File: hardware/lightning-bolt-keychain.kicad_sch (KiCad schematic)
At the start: 14 parts, among them J1 USB-C Power In

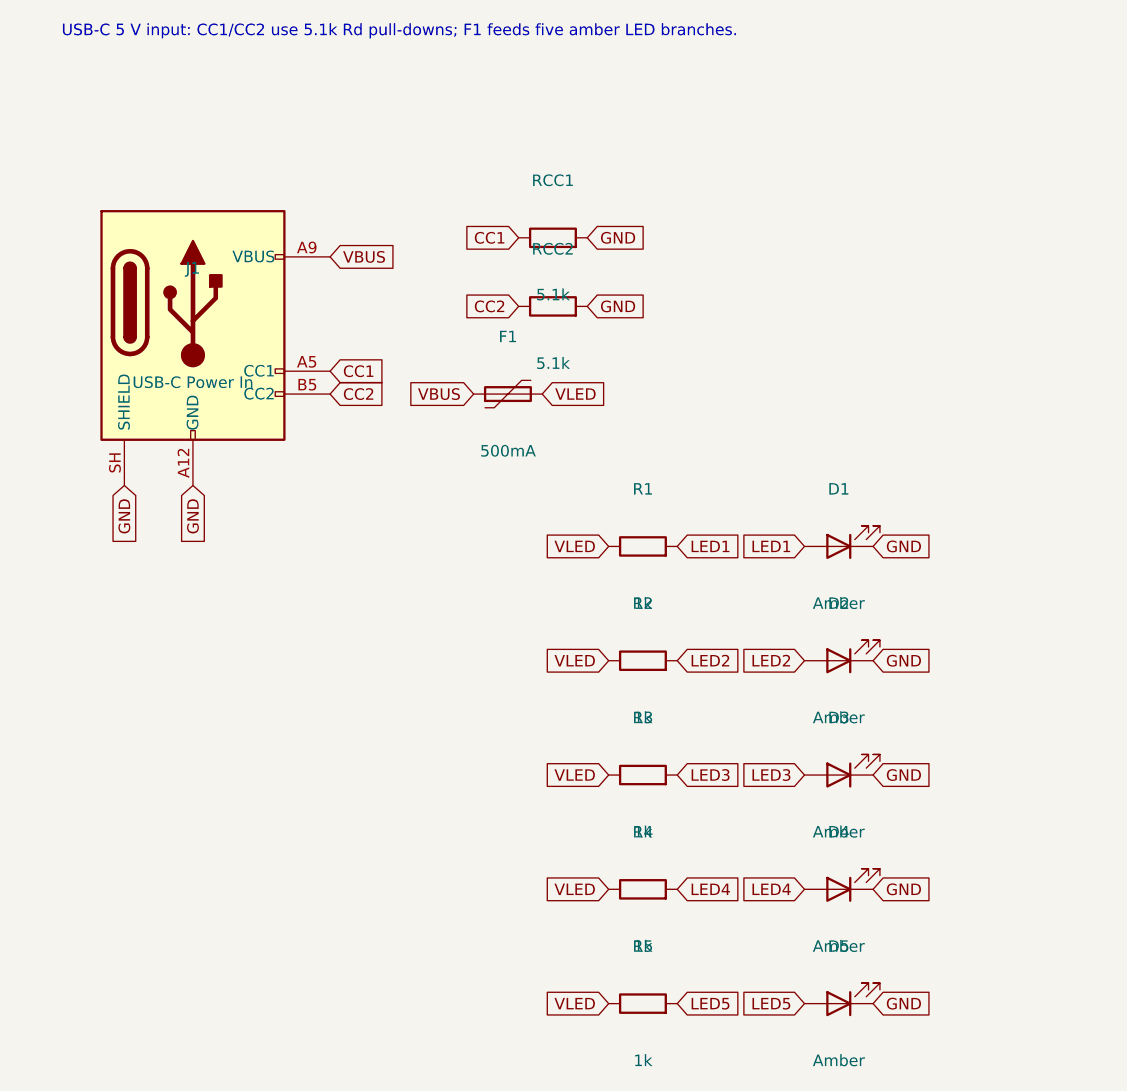
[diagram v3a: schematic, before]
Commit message: Refine bolt outline and schematic readability
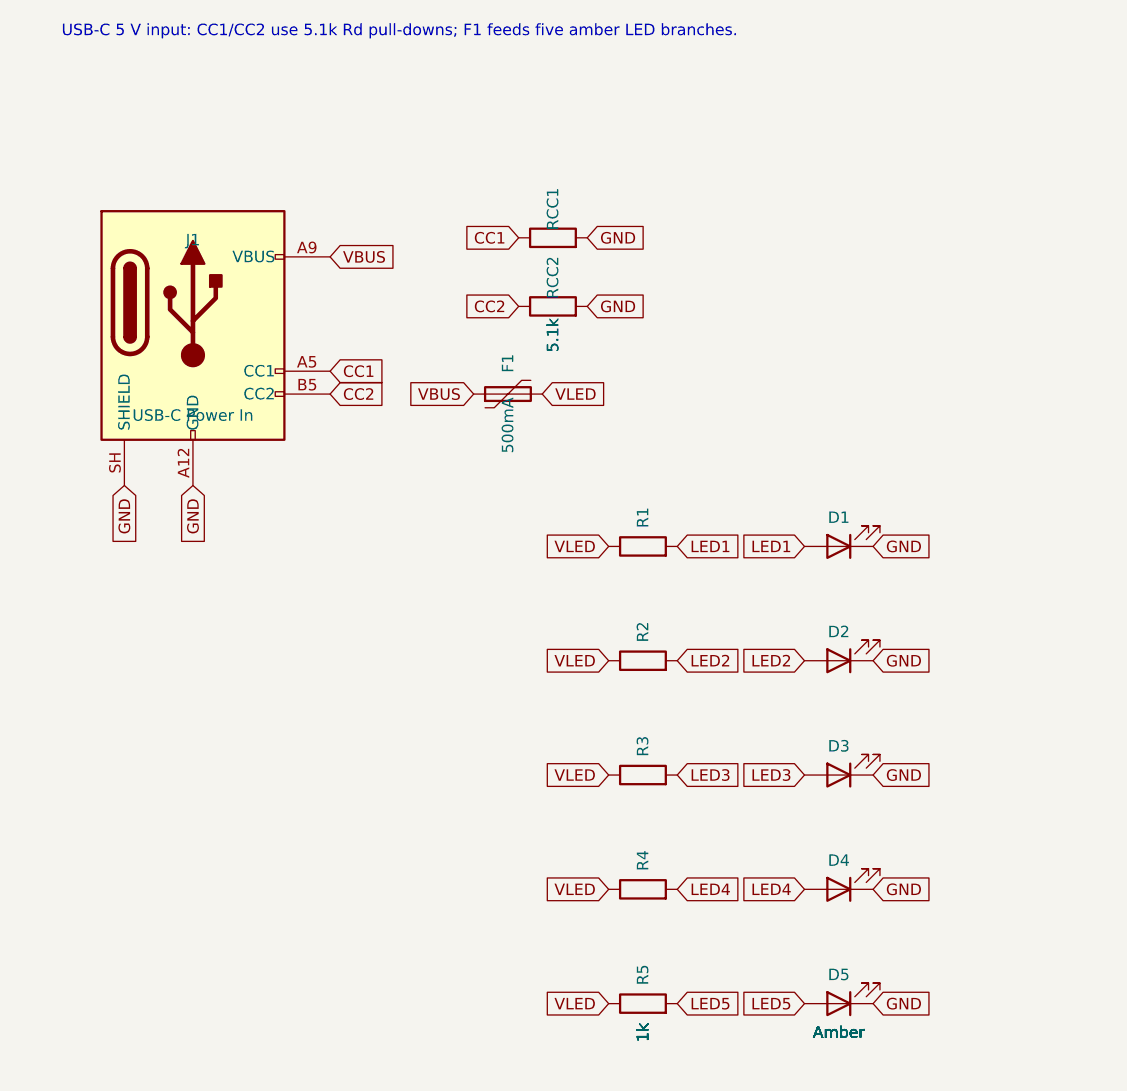
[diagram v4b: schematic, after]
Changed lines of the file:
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@@
   (symbol (lib_id "Connector:USB_C_Receptacle_PowerOnly_6P") (at 40.00 58.00 0) (unit 1)
     (in_bom yes) (on_board yes) (dnp no)
-    (property "Reference" "J1" (at 40.00 51.65 0)
+    (property "Reference" "J1" (at 40.00 48.50 0)
       (effects (font (size 1.27 1.27)))
     )
-    (property "Value" "USB-C Power In" (at 40.00 64.35 0)
+    (property "Value" "USB-C Power In" (at 40.00 68.00 0)
       (effects (font (size 1.27 1.27)))
     )
@@
   (symbol (lib_id "Device:Polyfuse") (at 75.00 65.62 90) (unit 1)
     (in_bom yes) (on_board yes) (dnp no)
-    (property "Reference" "F1" (at 75.00 59.27 90)
+    (property "Reference" "F1" (at 75.00 62.20 0)
       (effects (font (size 1.27 1.27)))
     )
-    (property "Value" "500mA" (at 75.00 71.97 90)
+    (property "Value" "500mA" (at 75.00 69.10 0)
       (effects (font (size 1.27 1.27)))
     )
@@
   (symbol (lib_id "Device:R") (at 80.00 48.26 90) (unit 1)
     (in_bom yes) (on_board yes) (dnp no)
-    (property "Reference" "RCC1" (at 80.00 41.91 90)
+    (property "Reference" "RCC1" (at 80.00 45.06 0)
       (effects (font (size 1.27 1.27)))
     )
-    (property "Value" "5.1k" (at 80.00 54.61 90)
+    (property "Value" "5.1k" (at 80.00 59.08 0)
       (effects (font (size 1.27 1.27)))
     )
@@
   (symbol (lib_id "Device:R") (at 80.00 55.88 90) (unit 1)
     (in_bom yes) (on_board yes) (dnp no)
-    (property "Reference" "RCC2" (at 80.00 49.53 90)
+    (property "Reference" "RCC2" (at 80.00 52.68 0)
       (effects (font (size 1.27 1.27)))
     )
-    (property "Value" "5.1k" (at 80.00 62.23 90)
+    (property "Value" "5.1k" (at 80.00 59.08 0)
       (effects (font (size 1.27 1.27)))
     )
@@
   (symbol (lib_id "Device:R") (at 90.00 82.55 90) (unit 1)
     (in_bom yes) (on_board yes) (dnp no)
-    (property "Reference" "R1" (at 90.00 76.20 90)
+    (property "Reference" "R1" (at 90.00 79.35 0)
       (effects (font (size 1.27 1.27)))
     )
-    (property "Value" "1k" (at 90.00 88.90 90)
+    (property "Value" "1k" (at 90.00 136.55 0)
       (effects (font (size 1.27 1.27)))
     )
@@
   (symbol (lib_id "Device:LED") (at 111.76 82.55 180) (unit 1)
     (in_bom yes) (on_board yes) (dnp no)
-    (property "Reference" "D1" (at 111.76 76.20 180)
+    (property "Reference" "D1" (at 111.76 79.35 0)
       (effects (font (size 1.27 1.27)))
     )
-    (property "Value" "Amber" (at 111.76 88.90 180)
+    (property "Value" "Amber" (at 111.76 136.55 0)
       (effects (font (size 1.27 1.27)))
     )
@@
   (symbol (lib_id "Device:R") (at 90.00 95.25 90) (unit 1)
     (in_bom yes) (on_board yes) (dnp no)
-    (property "Reference" "R2" (at 90.00 88.90 90)
+    (property "Reference" "R2" (at 90.00 92.05 0)
       (effects (font (size 1.27 1.27)))
     )
-    (property "Value" "1k" (at 90.00 101.60 90)
+    (property "Value" "1k" (at 90.00 136.55 0)
       (effects (font (size 1.27 1.27)))
     )
@@
   (symbol (lib_id "Device:LED") (at 111.76 95.25 180) (unit 1)
     (in_bom yes) (on_board yes) (dnp no)
-    (property "Reference" "D2" (at 111.76 88.90 180)
+    (property "Reference" "D2" (at 111.76 92.05 0)
       (effects (font (size 1.27 1.27)))
     )
-    (property "Value" "Amber" (at 111.76 101.60 180)
+    (property "Value" "Amber" (at 111.76 136.55 0)
       (effects (font (size 1.27 1.27)))
     )
@@
   (symbol (lib_id "Device:R") (at 90.00 107.95 90) (unit 1)
     (in_bom yes) (on_board yes) (dnp no)
-    (property "Reference" "R3" (at 90.00 101.60 90)
+    (property "Reference" "R3" (at 90.00 104.75 0)
       (effects (font (size 1.27 1.27)))
     )
-    (property "Value" "1k" (at 90.00 114.30 90)
+    (property "Value" "1k" (at 90.00 136.55 0)
       (effects (font (size 1.27 1.27)))
     )
@@
   (symbol (lib_id "Device:LED") (at 111.76 107.95 180) (unit 1)
     (in_bom yes) (on_board yes) (dnp no)
-    (property "Reference" "D3" (at 111.76 101.60 180)
+    (property "Reference" "D3" (at 111.76 104.75 0)
       (effects (font (size 1.27 1.27)))
     )
-    (property "Value" "Amber" (at 111.76 114.30 180)
+    (property "Value" "Amber" (at 111.76 136.55 0)
       (effects (font (size 1.27 1.27)))
     )
@@
   (symbol (lib_id "Device:R") (at 90.00 120.65 90) (unit 1)
     (in_bom yes) (on_board yes) (dnp no)
-    (property "Reference" "R4" (at 90.00 114.30 90)
+    (property "Reference" "R4" (at 90.00 117.45 0)
       (effects (font (size 1.27 1.27)))
     )
-    (property "Value" "1k" (at 90.00 127.00 90)
+    (property "Value" "1k" (at 90.00 136.55 0)
       (effects (font (size 1.27 1.27)))
     )
@@
   (symbol (lib_id "Device:LED") (at 111.76 120.65 180) (unit 1)
     (in_bom yes) (on_board yes) (dnp no)
-    (property "Reference" "D4" (at 111.76 114.30 180)
+    (property "Reference" "D4" (at 111.76 117.45 0)
       (effects (font (size 1.27 1.27)))
     )
-    (property "Value" "Amber" (at 111.76 127.00 180)
+    (property "Value" "Amber" (at 111.76 136.55 0)
       (effects (font (size 1.27 1.27)))
     )
@@
   (symbol (lib_id "Device:R") (at 90.00 133.35 90) (unit 1)
     (in_bom yes) (on_board yes) (dnp no)
-    (property "Reference" "R5" (at 90.00 127.00 90)
+    (property "Reference" "R5" (at 90.00 130.15 0)
       (effects (font (size 1.27 1.27)))
     )
-    (property "Value" "1k" (at 90.00 139.70 90)
+    (property "Value" "1k" (at 90.00 136.55 0)
       (effects (font (size 1.27 1.27)))
     )
@@
   (symbol (lib_id "Device:LED") (at 111.76 133.35 180) (unit 1)
     (in_bom yes) (on_board yes) (dnp no)
-    (property "Reference" "D5" (at 111.76 127.00 180)
+    (property "Reference" "D5" (at 111.76 130.15 0)
       (effects (font (size 1.27 1.27)))
     )
-    (property "Value" "Amber" (at 111.76 139.70 180)
+    (property "Value" "Amber" (at 111.76 136.55 0)
       (effects (font (size 1.27 1.27)))
     )
